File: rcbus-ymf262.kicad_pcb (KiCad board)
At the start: 2 copper layers, 100 x 50 mm, 42 parts, among them CON1 SJ1-3523N, P1 RC2014 BUS, U1 74HCT688, U2 YMF262, U5 YAC512, U6 TL074, X1 14.318MHz

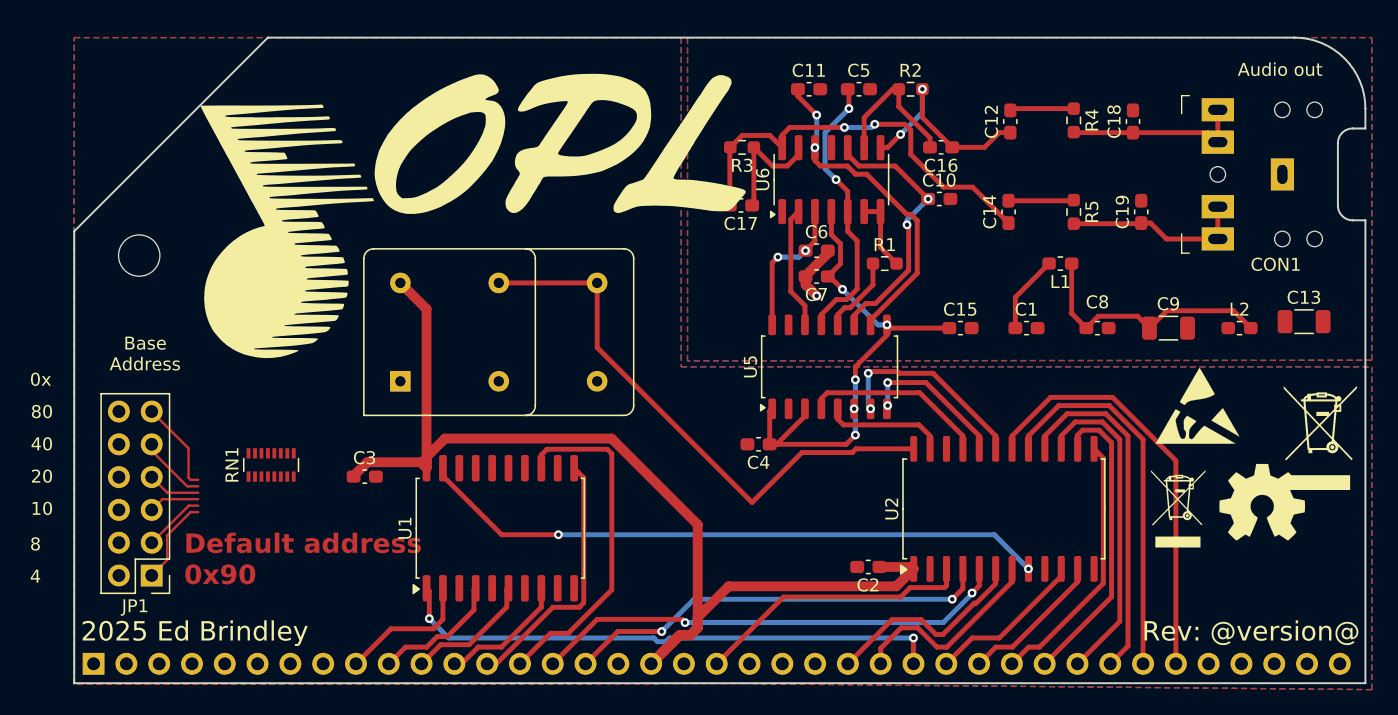
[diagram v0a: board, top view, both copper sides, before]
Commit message: some more routing, use individual resistors, change name to rcbus
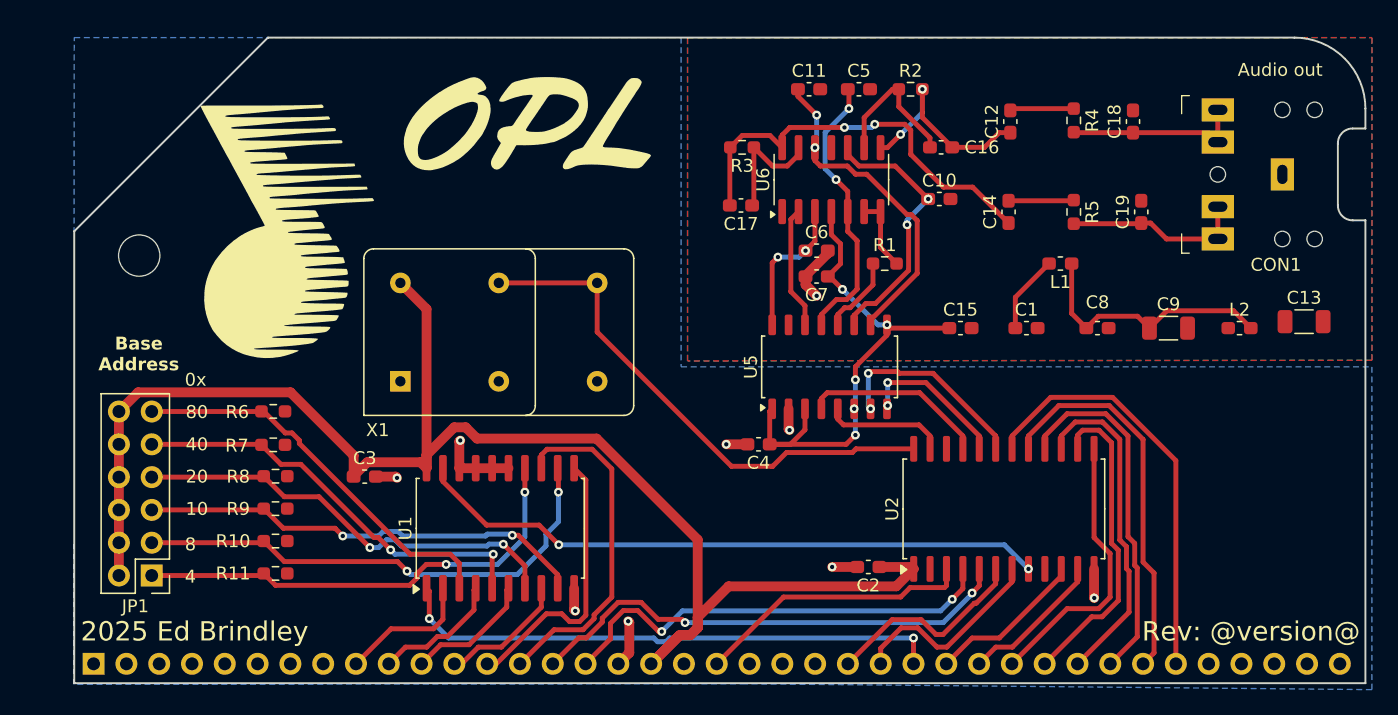
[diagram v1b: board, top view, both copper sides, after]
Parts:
- removed G2: LOGO, local:opl
- removed REF**: ESD-Logo_6.6x6mm_SilkScreen, Symbol:ESD-Logo_6.6x6mm_SilkScreen
- removed REF**: WEEE-Logo_5.6x8mm_SilkScreen, Symbol:WEEE-Logo_5.6x8mm_SilkScreen
- removed REF**: WEEE-Logo_4.2x6mm_SilkScreen, Symbol:WEEE-Logo_4.2x6mm_SilkScreen
- removed REF**: OSHW-Symbol_6.7x6mm_SilkScreen, Symbol:OSHW-Symbol_6.7x6mm_SilkScreen
- removed RN1: 10K, Resistor_SMD:R_Array_Convex_8x0602
- added G***: LOGO, electrified:opl, F.Cu at (95.5, 121.0)
- added R10: R_Small, Resistor_SMD:R_0603_1608Metric_Pad0.98x0.95mm_HandSolder, F.Cu at (76.1, 153.5)
- added R11: R_Small, Resistor_SMD:R_0603_1608Metric_Pad0.98x0.95mm_HandSolder, F.Cu at (76.1, 156.0)
- added R6: R_Small, Resistor_SMD:R_0603_1608Metric_Pad0.98x0.95mm_HandSolder, F.Cu at (75.9, 143.4)
- added R7: R_Small, Resistor_SMD:R_0603_1608Metric_Pad0.98x0.95mm_HandSolder, F.Cu at (75.9, 146.0)
- added R8: R_Small, Resistor_SMD:R_0603_1608Metric_Pad0.98x0.95mm_HandSolder, F.Cu at (76.1, 148.5)
- added R9: R_Small, Resistor_SMD:R_0603_1608Metric_Pad0.98x0.95mm_HandSolder, F.Cu at (76.1, 151.0)
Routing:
- net VCC: track 86.1 -> 121.3 mm
- net Net-(JP1-Pin_3): track 4.79 -> 38.8 mm, vias 0 -> 2
- net Net-(JP1-Pin_5): track 3.94 -> 34.9 mm, vias 0 -> 2
- net Net-(JP1-Pin_7): track 4.10 -> 34.1 mm, vias 0 -> 2
- net Net-(JP1-Pin_1): track 6.75 -> 36.2 mm, vias 0 -> 2
- net Net-(JP1-Pin_9): track 5.24 -> 32.6 mm, vias 0 -> 2
- net Net-(JP1-Pin_11): track 7.13 -> 30.8 mm
- net GND: track 4.57 -> 25.2 mm, vias 1 -> 9
- net /CLK: track 43.8 -> 40.8 mm
- net /A0: track 33.2 -> 35.2 mm
- net /D2: track 20.4 -> 21.7 mm
- net /A3: track 20.2 -> 21.5 mm
- net /A1: track 37.1 -> 38.4 mm
- net /D3: track 23.5 -> 24.4 mm
- net Net-(U6D--): track 9.53 -> 8.78 mm
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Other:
- board text added: "github.com/electrified/rcbus-ymf262"
- board text removed: "Default address 0x90"
- board text removed: "github.com/electrified/rc2014-ymf262"

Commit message: fully routed - first attempt
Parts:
- added G3: OSHW-Symbol_6.7x6mm_SilkScreen, Symbol:OSHW-Symbol_6.7x6mm_SilkScreen, B.Cu at (155.0, 151.0)
- added G4: ESD-Logo_6.6x6mm_SilkScreen, Symbol:ESD-Logo_6.6x6mm_SilkScreen, B.Cu at (155.5, 144.0)
- G1: footprint local:adlib -> electrified:adlib2
- moved G1 6.82 mm to (79.6, 123.2)
- renumbered G*** to G2
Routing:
- net GND: track 25.2 -> 60.6 mm, vias 9 -> 26
- net +5VA: track 40.3 -> 66.7 mm, vias 5 -> 2
- net Net-(U5-MP): track 9.48 -> 18.9 mm
- net Net-(C8-Pad1): track 20.1 -> 23.1 mm
- net Net-(U5-AOUT): track 21.6 -> 24.3 mm
- net /DAC_CLK: track 9.49 -> 11.9 mm
- net /SMPBD: track 15.8 -> 14.5 mm, vias 2 -> 0
- net Net-(U5-CH1): track 25.2 -> 26.2 mm
- net /CLK: track 40.8 -> 41.6 mm
- net Net-(JP1-Pin_11): track 30.8 -> 31.6 mm
- net /DOAB: track 14.3 -> 14.7 mm, vias 0 -> 2
- net /SMPAC: track 11.6 -> 11.4 mm, vias 2 -> 0
- net Net-(U5-CV): vias 2 -> 0
- removed copper zone on F.Cu, net GND

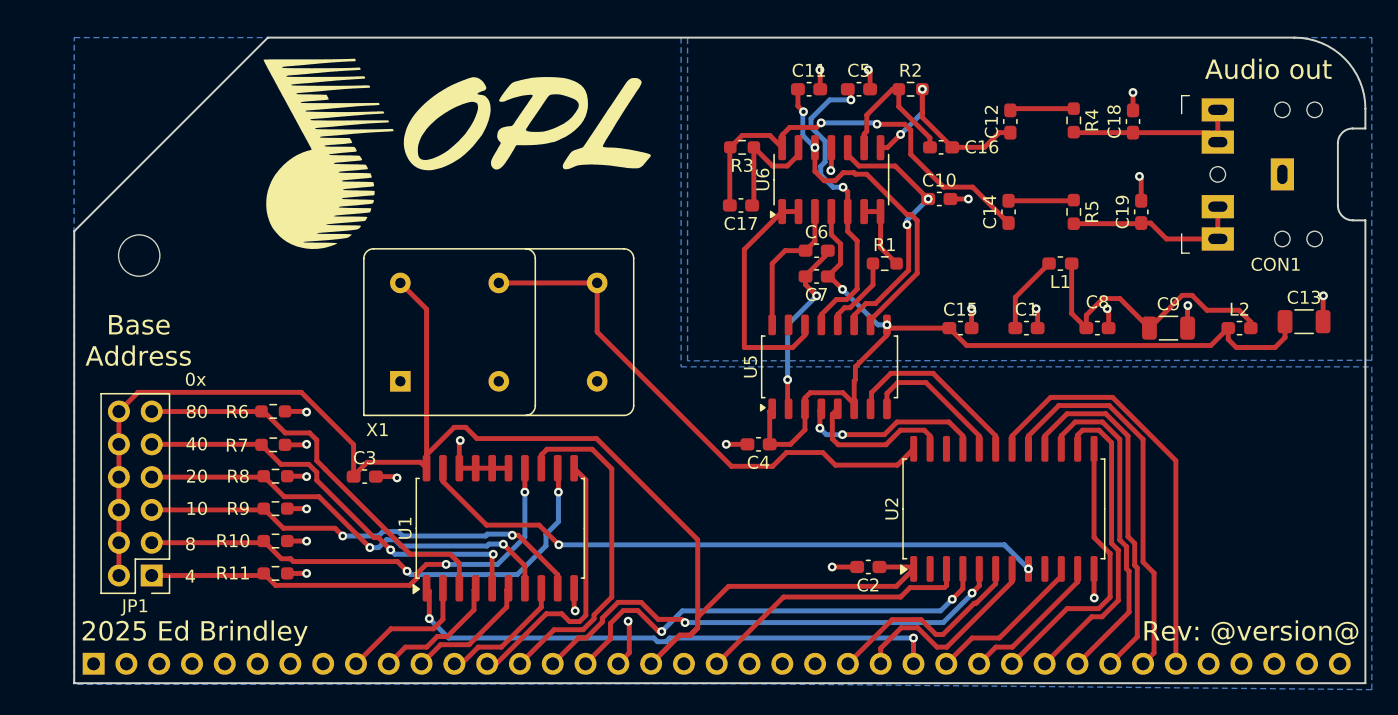
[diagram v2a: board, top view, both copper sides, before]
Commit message: move some vias out of pads
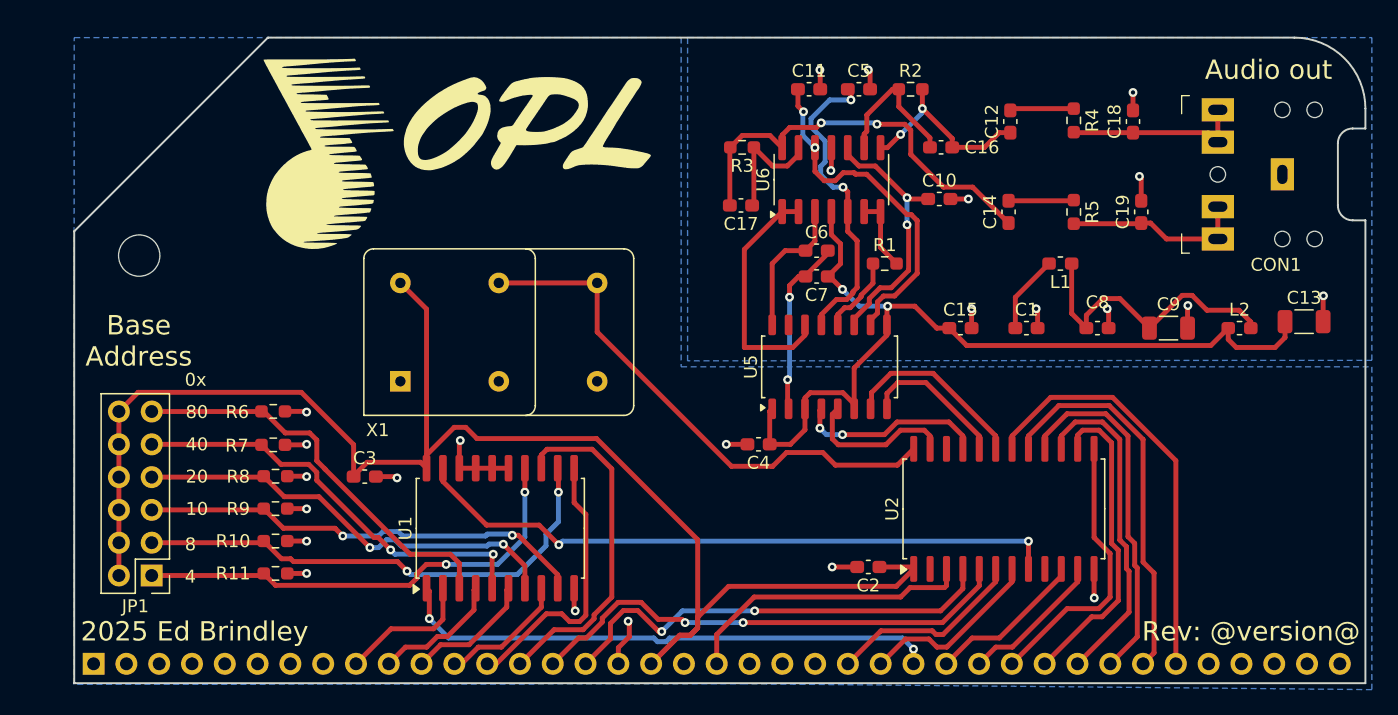
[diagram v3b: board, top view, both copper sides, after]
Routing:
- net /L: track 16.6 -> 15.1 mm
- net /~{CS}: track 49.2 -> 50.7 mm
- net +5VA: track 66.7 -> 68.1 mm
- net /~{RD}: track 15.7 -> 14.3 mm
- net /~{RESET}: track 21.6 -> 22.9 mm
- net /~{WR}: track 16.1 -> 15.3 mm
- net Net-(U5-CH2): track 20.3 -> 19.8 mm
- net /~{IORQ}: track 42.8 -> 42.3 mm
- net Net-(U5-CH1): track 26.2 -> 26.7 mm

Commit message: reroute
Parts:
- moved C2 11.9 mm to (110.3, 157.6)
- moved U2 11.0 mm to (121.5, 152.0)
- moved G3 7.16 mm to (156.5, 158.0)
- moved U1 6.94 mm to (86.6, 151.8)
- moved G1 6.69 mm to (75.5, 128.5)
- moved G4 6.58 mm to (156.5, 150.5)
- moved C3 5.07 mm to (79.3, 145.0)
- moved C4 4.51 mm to (110.0, 143.2)
- moved X1 2.72 mm to (94.5, 135.0)
- moved G2 2.50 mm to (93.0, 121.0)
- moved R10 1.78 mm to (74.3, 153.5)
- moved R11 1.78 mm to (74.3, 156.0)
- moved R8 1.78 mm to (74.3, 148.5)
- moved R9 1.78 mm to (74.3, 151.0)
- moved R6 1.78 mm to (74.1, 143.5)
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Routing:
- net GND: track 60.2 -> 141.9 mm, vias 26 -> 16
- net VCC: track 121.8 -> 95.3 mm, vias 0 -> 1
- net /~{RESET}: track 22.9 -> 9.84 mm
- net /A0: track 35.2 -> 22.2 mm
- net /A1: track 38.3 -> 26.7 mm
- net /DOAB: track 14.7 -> 4.12 mm, vias 2 -> 0
- net /~{IORQ}: track 42.3 -> 52.2 mm
- net /SMPBD: track 14.5 -> 4.73 mm, vias 0 -> 2
- net /CLK: track 41.6 -> 32.8 mm
- net /~{WR}: track 15.3 -> 6.53 mm
- net Net-(JP1-Pin_3): track 38.8 -> 30.7 mm
- net /~{RD}: track 14.3 -> 6.69 mm
- net Net-(JP1-Pin_1): track 36.2 -> 28.7 mm
- net Net-(JP1-Pin_7): track 34.1 -> 27.4 mm, vias 2 -> 0
- net Net-(U5-MP): track 18.9 -> 12.6 mm, vias 0 -> 2
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
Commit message: more routing
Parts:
- removed G3: OSHW-Symbol_6.7x6mm_SilkScreen, Symbol:OSHW-Symbol_6.7x6mm_SilkScreen
- removed G4: ESD-Logo_6.6x6mm_SilkScreen, Symbol:ESD-Logo_6.6x6mm_SilkScreen
- R10, R11, R6, R7, R8, R9: value R_Small -> 10K
- moved C14 11.1 mm to (132.0, 116.9)
- moved C19 11.1 mm to (142.2, 116.9)
- moved R5 11.1 mm to (137.0, 116.9)
- moved C5 11.1 mm to (126.0, 128.5), turned to -90 degrees
- moved C10 11.0 mm to (120.5, 118.5), turned to 90 degrees
- moved C1 10.4 mm to (134.2, 147.4)
- moved C13 10.4 mm to (155.7, 146.9)
- moved C8 10.4 mm to (139.7, 147.4)
- moved C9 10.4 mm to (145.2, 147.4)
- moved L1 10.4 mm to (136.8, 142.4)
- moved L2 10.4 mm to (150.7, 147.4)
- moved C17 8.42 mm to (114.8, 119.5)
- moved R3 6.09 mm to (114.8, 117.5)
- moved C16 5.22 mm to (125.0, 118.5), turned to -90 degrees
- moved C15 2.65 mm to (126.5, 136.8)
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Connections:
- net Net-(U5-CH1) renamed /AUDIO_CH1
- net Net-(U5-CH2) renamed /AUDIO_CH2
- C1 pad 1: +5V -> VCC
- L1 pad 2: +5V -> VCC
- R10 pad 1: GND -> Net-(JP1-Pin_3)
- R10 pad 2: Net-(JP1-Pin_3) -> GND
- R11 pad 1: GND -> Net-(JP1-Pin_1)
- R11 pad 2: Net-(JP1-Pin_1) -> GND
- R6 pad 1: GND -> Net-(JP1-Pin_11)
- R6 pad 2: Net-(JP1-Pin_11) -> GND
- R7 pad 1: GND -> Net-(JP1-Pin_9)
- R7 pad 2: Net-(JP1-Pin_9) -> GND
- R8 pad 1: GND -> Net-(JP1-Pin_7)
- R8 pad 2: Net-(JP1-Pin_7) -> GND
- R9 pad 1: GND -> Net-(JP1-Pin_5)
- R9 pad 2: Net-(JP1-Pin_5) -> GND
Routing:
- net GND: track 141.9 -> 79.5 mm, vias 16 -> 18
- net Net-(C19-Pad1): track 13.6 -> 28.0 mm
- net +5VA: track 70.0 -> 59.5 mm, vias 4 -> 1
- net Net-(U5-AOUT): track 26.1 -> 16.9 mm, vias 2 -> 0
- net /R: track 34.9 -> 25.7 mm, vias 4 -> 0
- net VCC: track 95.3 -> 101.6 mm
- net /D7: track 30.8 -> 37.0 mm, vias 1 -> 0
- net /D5: track 24.0 -> 30.2 mm, vias 1 -> 0
- net +5V: track 6.08 -> 0.00 mm
- net /D6: track 28.0 -> 33.4 mm
- net /SMPBD: track 4.73 -> 10.1 mm, vias 2 -> 0
- net Net-(U6D--): track 11.2 -> 5.97 mm
- net Net-(U6C--): track 11.4 -> 6.33 mm
- net /D4: track 22.1 -> 27.0 mm, vias 1 -> 0
- net Net-(U5-MP): track 12.6 -> 16.3 mm, vias 2 -> 0
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- added copper zone on F.Cu, net GND

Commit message: pcb updates, remove old github actions
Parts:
- removed the C15 at (126.5, 136.8)
- renumbered C2 to C1, C11 to C10, C5 to C11, C7 to C12, C16 to C13, C17 to C14, C12 to C15, C14 to C16, C18 to C17, C19 to C18, C1 to C2, C8 to C3, C9 to C4, C13 to C5, C3 to C6, C4 to C7, C6 to C8, C10 to C9, R6 to R1, R4 to R10, R5 to R11, R7 to R2, R8 to R3, R9 to R4, R10 to R5, R11 to R6, R1 to R7, R2 to R8, R3 to R9, U5 to U3, U6 to U4
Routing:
- net +5VA: track 59.5 -> 57.3 mm
